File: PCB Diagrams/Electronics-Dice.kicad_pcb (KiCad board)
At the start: 2 copper layers, 142.2 x 59.7 mm, 31 parts, among them J1 01x02, J2 01x02, J3 01x10_Pin, J4 01x10_Pin, SW1 SW_Push, SW2 SW_SPST, SW3 SPDT_Slide, U1 Arduino_Nano_v3

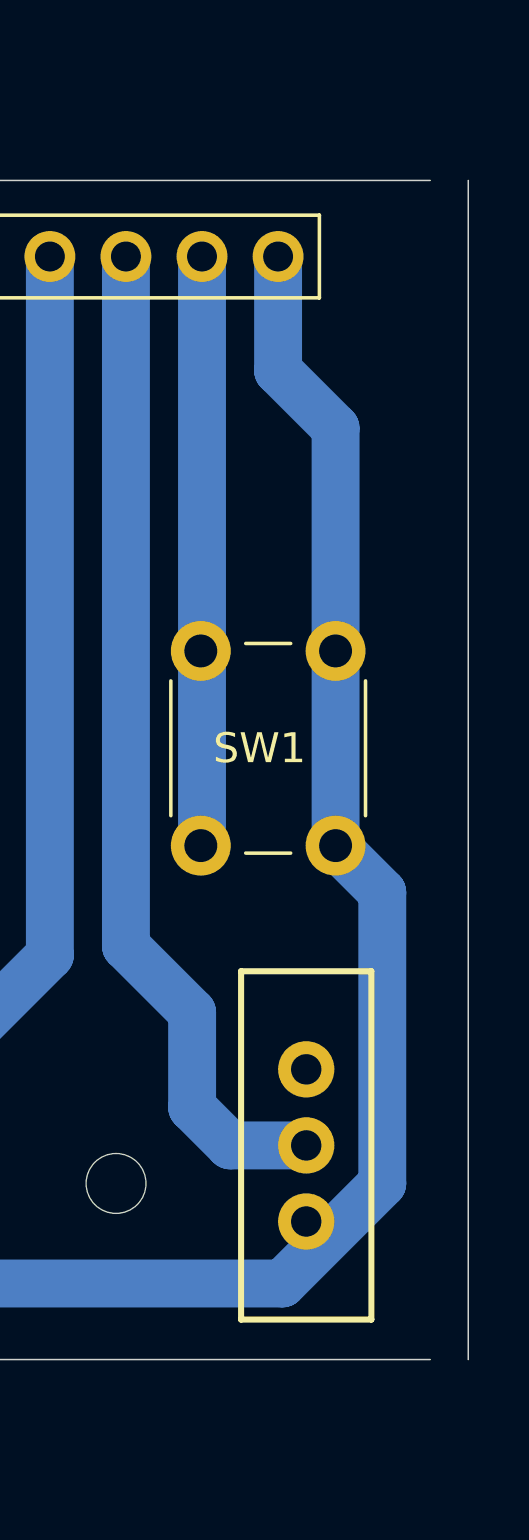
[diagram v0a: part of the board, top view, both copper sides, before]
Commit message: Adding KiCAD 9 schematics and PCB diagrams
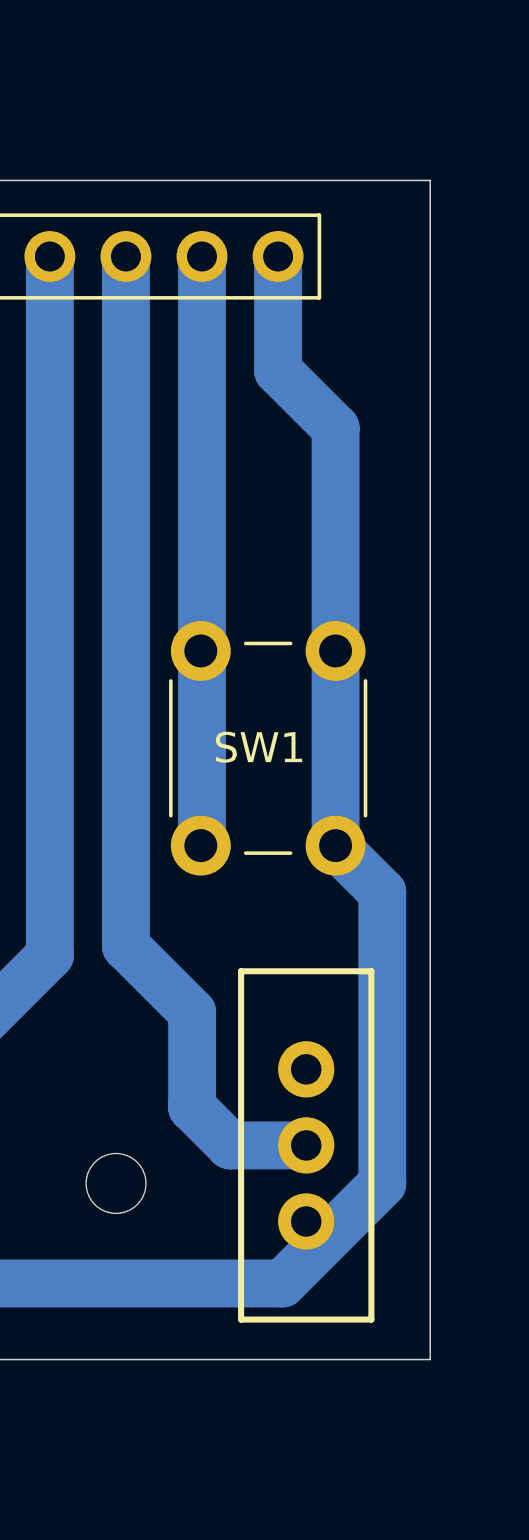
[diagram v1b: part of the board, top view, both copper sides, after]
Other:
- board size 142.2 x 59.7 mm -> 141 x 59.7 mm
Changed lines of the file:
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@@
 	)
 	(gr_line
-		(start 222.25 73.19)
-		(end 222.25 112.56)
+		(start 220.98 73.19)
+		(end 220.98 112.56)
 		(stroke
 			(width 0.05)
